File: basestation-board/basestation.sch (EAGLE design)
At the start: 68 parts, among them IC1 STM32F0, IC2 MCP1700TT, IC3 MCP73831, IC4 MCP1700TT, J2 SWD_PTH_SHROUD, Q1 BSS84, Q2 BSS84, SW1 ROTARTY_ENCODER, U1 RFM98, U2 NHD-C0216CIZ-FSW, U3 RN4020, X1 BU-SMA-V, X2 CRYSTAL-GROUNDED

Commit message: minor changes
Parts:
- added U$1: MMBZ27VCLT1, SparkFun-DiscreteSemi:MMBZ27VCLT1
- added U$2: NUP2114UCMR6T1G, Mine:NUP2114UCMR6T1G
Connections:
- new net R_INT: IC1.PB15, U1.DIO0
- net DM: now also U$2.IO1
- net DP: now also U$2.IO2
- net GND: now also U$2.VN
- net N$1: now also U$1.C
- net N$35: now also U$2.VP
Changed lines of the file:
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@@
 <part name="C17" library="resistor" deviceset="C-EU" device="C0603" value="100n"/>
 <part name="GND42" library="supply1" deviceset="GND" device=""/>
+<part name="U$1" library="SparkFun-DiscreteSemi" deviceset="MMBZ27VCLT1" device=""/>
+<part name="U$2" library="Mine" deviceset="NUP2114UCMR6T1G" device=""/>
+<part name="GND43" library="supply1" deviceset="GND" device=""/>
 </parts>
 <sheets>
@@
 <instance part="C17" gate="G$1" x="12.7" y="190.5" rot="R180"/>
 <instance part="GND42" gate="1" x="12.7" y="185.42"/>
+<instance part="U$1" gate="G$1" x="35.56" y="187.96" rot="R180"/>
+<instance part="U$2" gate="G$1" x="167.64" y="73.66"/>
+<instance part="GND43" gate="1" x="167.64" y="55.88"/>
 </instances>
 <busses>
@@
 <pinref part="U1" gate="G$1" pin="ANT"/>
 <pinref part="X1" gate="G$1" pin="1"/>
+<pinref part="U$1" gate="G$1" pin="C"/>
+<wire x1="35.56" y1="180.34" x2="35.56" y2="172.72" width="0.1524" layer="91"/>
+<junction x="35.56" y="172.72"/>
 </segment>
 </net>
@@
 <pinref part="GND42" gate="1" pin="GND"/>
 </segment>
+<segment>
+<pinref part="U$2" gate="G$1" pin="VN"/>
+<pinref part="GND43" gate="1" pin="GND"/>
+</segment>
 </net>
 <net name="VBAT_S" class="0">
@@
 <label x="119.38" y="68.58" size="1.778" layer="95"/>
 </segment>
+<segment>
+<label x="147.32" y="76.2" size="1.778" layer="95"/>
+<pinref part="U$2" gate="G$1" pin="IO1"/>
+<wire x1="157.48" y1="76.2" x2="142.24" y2="76.2" width="0.1524" layer="91"/>
+</segment>
 </net>
 <net name="DP" class="0">
@@
 <wire x1="129.54" y1="66.04" x2="116.84" y2="66.04" width="0.1524" layer="91"/>
 <label x="119.38" y="66.04" size="1.778" layer="95"/>
+</segment>
+<segment>
+<wire x1="157.48" y1="71.12" x2="142.24" y2="71.12" width="0.1524" layer="91"/>
+<label x="147.32" y="71.12" size="1.778" layer="95"/>
+<pinref part="U$2" gate="G$1" pin="IO2"/>
 </segment>
 </net>
@@
 <net name="N$35" class="0">
 <segment>
+<label x="149.86" y="88.9" size="1.778" layer="95"/>
+<pinref part="U$2" gate="G$1" pin="VP"/>
+<wire x1="129.54" y1="88.9" x2="167.64" y2="88.9" width="0.1524" layer="91"/>
 <pinref part="L1" gate="G$1" pin="2"/>
 <pinref part="JP1" gate="G$1" pin="VCC"/>
 <wire x1="121.92" y1="71.12" x2="129.54" y2="71.12" width="0.1524" layer="91"/>
+<wire x1="129.54" y1="88.9" x2="129.54" y2="71.12" width="0.1524" layer="91"/>
 </segment>
 </net>
@@
 </segment>
 </net>
+<net name="R_INT" class="0">
+<segment>
+<pinref part="U1" gate="G$1" pin="DIO0"/>
+<wire x1="35.56" y1="165.1" x2="43.18" y2="165.1" width="0.1524" layer="91"/>
+<label x="35.56" y="165.1" size="1.778" layer="95"/>
+</segment>
+<segment>
+<pinref part="IC1" gate="G$1" pin="PB15"/>
+<wire x1="43.18" y1="35.56" x2="55.88" y2="35.56" width="0.1524" layer="91"/>
+<label x="48.26" y="35.56" size="1.778" layer="95"/>
+</segment>
+</net>

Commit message: some stuff changed lol
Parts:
- removed R16: (no value), resistor:R-EU_R0603
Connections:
- net GND: no longer R16.2
- net N$28: no longer R16.1
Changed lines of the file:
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@@
 <part name="R15" library="resistor" deviceset="R-EU_" device="R0603"/>
 <part name="GND32" library="supply1" deviceset="GND" device=""/>
-<part name="R16" library="resistor" deviceset="R-EU_" device="R0603"/>
 <part name="GND33" library="supply1" deviceset="GND" device=""/>
 <part name="X2" library="SparkFun-FreqCtrl" deviceset="CRYSTAL-GROUNDED" device=""/>
@@
 <instance part="R15" gate="G$1" x="86.36" y="119.38" rot="R90"/>
 <instance part="GND32" gate="1" x="86.36" y="111.76"/>
-<instance part="R16" gate="G$1" x="121.92" y="63.5" rot="R180"/>
 <instance part="GND33" gate="1" x="114.3" y="58.42"/>
 <instance part="X2" gate="G$1" x="55.88" y="15.24" rot="R90"/>
@@
 </segment>
 <segment>
-<pinref part="R16" gate="G$1" pin="2"/>
 <wire x1="116.84" y1="63.5" x2="114.3" y2="63.5" width="0.1524" layer="91"/>
 <wire x1="114.3" y1="63.5" x2="114.3" y2="60.96" width="0.1524" layer="91"/>
@@
 <segment>
 <pinref part="JP1" gate="G$1" pin="ID"/>
-<pinref part="R16" gate="G$1" pin="1"/>
 <wire x1="129.54" y1="63.5" x2="127" y2="63.5" width="0.1524" layer="91"/>
 </segment>

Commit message: proded silk
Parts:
- removed U$1: MMBZ27VCLT1, SparkFun-DiscreteSemi:MMBZ27VCLT1
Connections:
- net N$1: no longer U$1.C
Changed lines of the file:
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@@
 <part name="C17" library="resistor" deviceset="C-EU" device="C0603" value="100n"/>
 <part name="GND42" library="supply1" deviceset="GND" device=""/>
-<part name="U$1" library="SparkFun-DiscreteSemi" deviceset="MMBZ27VCLT1" device=""/>
 <part name="U$2" library="Mine" deviceset="NUP2114UCMR6T1G" device=""/>
 <part name="GND43" library="supply1" deviceset="GND" device=""/>
@@
 <instance part="C17" gate="G$1" x="12.7" y="190.5" rot="R180"/>
 <instance part="GND42" gate="1" x="12.7" y="185.42"/>
-<instance part="U$1" gate="G$1" x="35.56" y="187.96" rot="R180"/>
 <instance part="U$2" gate="G$1" x="167.64" y="73.66"/>
 <instance part="GND43" gate="1" x="167.64" y="55.88"/>
@@
 <pinref part="U1" gate="G$1" pin="ANT"/>
 <pinref part="X1" gate="G$1" pin="1"/>
-<pinref part="U$1" gate="G$1" pin="C"/>
-<wire x1="35.56" y1="180.34" x2="35.56" y2="172.72" width="0.1524" layer="91"/>
-<junction x="35.56" y="172.72"/>
 </segment>
 </net>

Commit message: adding stuff to silk
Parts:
- C10, C13, C9: value 4u7 -> (none)
- C11: value 4u7 -> 100n
- C14, C16, C7: value (none) -> 4u7
- C17: value 100n -> 4u7
- J1: value (none) -> SWD_PTH_SHROUD; device dtb:JST_2MM_MALE -> dtb:SWD_PTH_SHROUD
- J2: value SWD_PTH_SHROUD -> (none); device dtb:SWD_PTH_SHROUD -> dtb:JST_2MM_MALE
- LED1: device led:LED5MM -> led:LEDCHIP-LED0805
- LED2: device led:LED3MM -> led:LED5MM
- LED4: device led:LEDCHIP-LED0805 -> led:LED3MM
- S1: value SWITCH-MOMENTARY-2SMD -> SWITCH-MOMENTARY-2PTH; device Mine:SWITCH-MOMENTARY-2SMD -> Mine:SWITCH-MOMENTARY-2PTH
- S3: value SWITCH-MOMENTARY-2PTH -> SWITCH-MOMENTARY-2SMD; device Mine:SWITCH-MOMENTARY-2PTH -> Mine:SWITCH-MOMENTARY-2SMD
- U1: value RFM98 -> NHD-C0216CIZ-FSW; device Mine:RFM98 -> dtb:NHD-C0216CIZ-FSW
- U2: value NHD-C0216CIZ-FSW -> RFM98; device dtb:NHD-C0216CIZ-FSW -> Mine:RFM98
- renumbered R18 to R16, U$2 to U$3, U$5 to U$1
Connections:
- removed net N$11 (its old number): LED1.C, R4.2
- new net N$10: LED4.C, R6.2
- net +3V3: now also C15.2, C17.2, C9.2, IC4.OUT, J1.VCC, R4.1, R5.1, S3.2, U1.VDD; no longer C13.2, C14.2, C6.2, IC2.OUT, J2.VCC, R6.1, R7.1, S1.2, U2.VDD
- net 3.3V: now also C11.2, C7.2, IC2.OUT, U2.3.3V; no longer C10.2, C17.2, IC4.OUT, U1.3.3V
- net AIN1: now also R11.2; no longer R15.2
- net GND: now also C14.1, J1.GND1, J1.GND2, J1.GNDD, J2.-, LED7.C, R11.1, R12.1, R6.1, S1.1, U1.K, U1.VSS, U2.GND; no longer C4.1, J1.-, J2.GND1, J2.GND2, J2.GNDD, LED4.C, R13.1, R15.1, R2.1, S3.1, U1.GND, U2.K, U2.VSS
- net LED1: now also LED3.A; no longer LED2.A
- net LED2: now also LED4.A; no longer LED3.A
- net LED3: now also LED2.A; no longer LED1.A
- net LED4: now also R2.1; no longer R4.1
- net MISO: now also U2.MISO; no longer U1.MISO
- net MOSI: now also U2.MOSI; no longer U1.MOSI
- net N$1: now also U2.ANT; no longer U1.ANT
- net N$12: now also C4.1, U1.VOUT; no longer C14.1, U2.VOUT
- net N$13: now also R8.2; no longer R11.2
- net N$15: now also LED7.A, R7.1; no longer LED5.A, R10.1
- net N$16: now also R8.1; no longer R11.1
- net N$17: now also LED5.A; no longer LED4.A
- net N$23: now also R13.1, U1.A; no longer R5.1, U2.A
- net N$27: now also R12.2, R15.1; no longer R12.1, R13.2
- net N$29: now also LED1.C; no longer LED7.C
- net N$3: now also R13.2; no longer R5.2
- net N$30: now also R10.2; no longer R17.2
- net N$31: now also C6.2; no longer C16.2
- net N$32: now also C10.2, R10.1; no longer C15.2, R17.1
- net N$33: now also C14.2, J2.+; no longer C8.2, J1.+
- net N$34: now also LED1.A, R17.2; no longer LED7.A, R8.2
- net N$4: now also S3.1; no longer S1.1
- net N$5: now also R7.2; no longer R10.2
- net N$8: now also U1.C1-; no longer U2.C1-
- net N$9: now also U1.C1+; no longer U2.C1+
- net NSS: now also U2.NSS; no longer U1.NSS
- net RST: now also J1.NRST; no longer J2.NRST
- net R_INT: now also U2.DIO0; no longer U1.DIO0
- net SCL: now also R4.2, U1.SCL; no longer R7.2, U2.SCL
- net SCLK: now also U2.SCK; no longer U1.SCK
- net SDA: now also R5.2, U1.SDA; no longer R6.2, U2.SDA
- net SW2: now also S1.2; no longer S3.2
- net SWCLK: now also J1.SWCLK; no longer J2.SWCLK
- net SWDAT: now also J1.SWDAT; no longer J2.SWDAT
- net VBAT_S: now also R15.2; no longer R12.2
- net VBUS: now also C16.2, R17.1; no longer C9.2, R8.1
- net VIN_S: now also C13.2, C8.2; no longer C11.2, C7.2
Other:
- moved on the sheet: C10, C11, C12, C13, C14, C15, C16, C17, C2, C3, C4, C5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

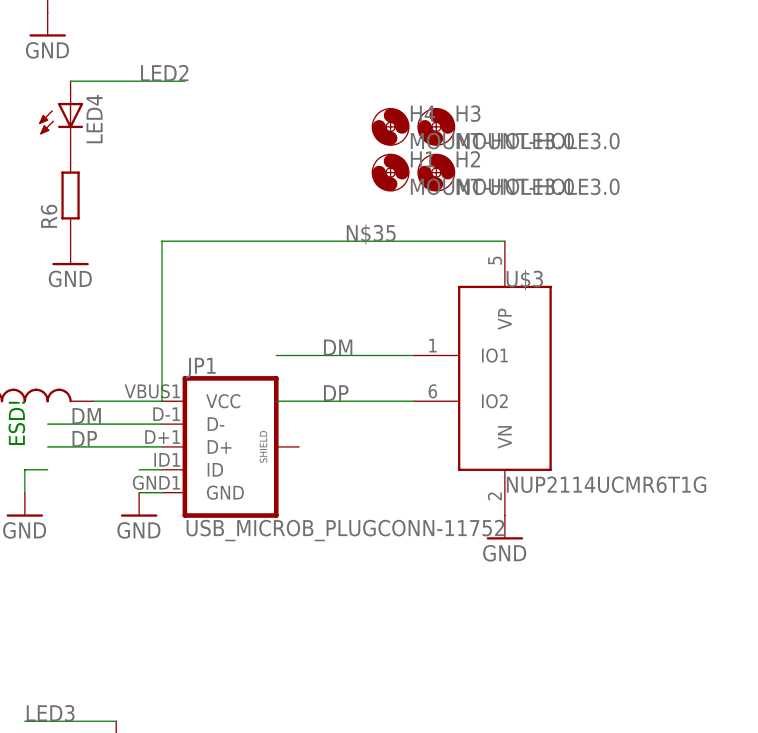
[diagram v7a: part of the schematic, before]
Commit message: added esd protection
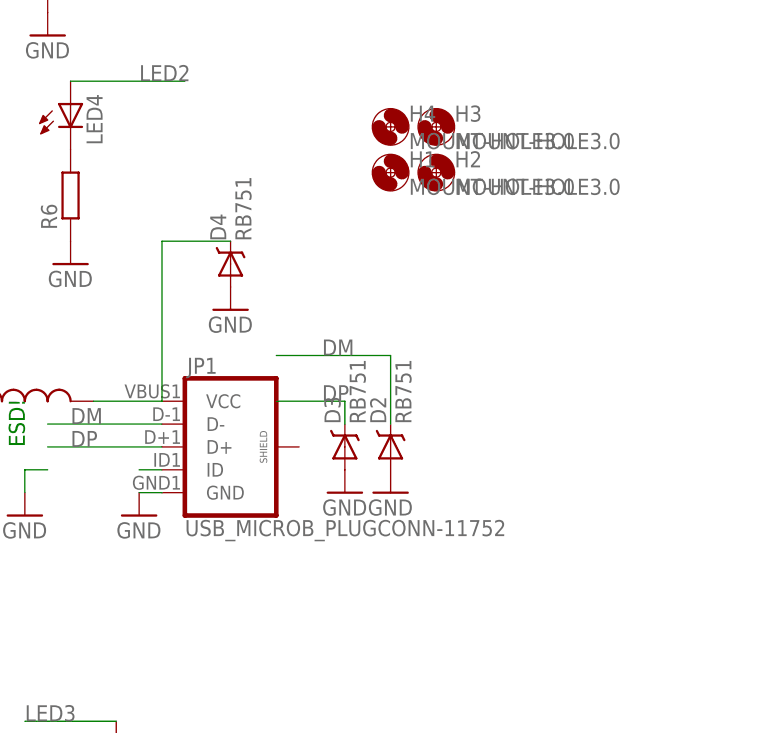
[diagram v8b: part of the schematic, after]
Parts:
- removed U$3: NUP2114UCMR6T1G, Mine:NUP2114UCMR6T1G
- added D2, D3, D4: RB751, SparkFun-DiscreteSemi:RB751
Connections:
- net DM: now also D2.C; no longer U$3.IO1
- net DP: now also D3.C; no longer U$3.IO2
- net GND: now also D2.A, D3.A, D4.A; no longer U$3.VN
- net N$35: now also D4.C; no longer U$3.VP
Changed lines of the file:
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@@
 <part name="C11" library="resistor" deviceset="C-EU" device="C0603" value="100n"/>
 <part name="GND42" library="supply1" deviceset="GND" device=""/>
-<part name="U$3" library="Mine" deviceset="NUP2114UCMR6T1G" device=""/>
-<part name="GND43" library="supply1" deviceset="GND" device=""/>
+<part name="GND44" library="supply1" deviceset="GND" device=""/>
+<part name="GND45" library="supply1" deviceset="GND" device=""/>
+<part name="D2" library="SparkFun-DiscreteSemi" deviceset="RB751" device="" value="RB751"/>
+<part name="D3" library="SparkFun-DiscreteSemi" deviceset="RB751" device="" value="RB751"/>
+<part name="D4" library="SparkFun-DiscreteSemi" deviceset="RB751" device="" value="RB751"/>
+<part name="GND46" library="supply1" deviceset="GND" device=""/>
 </parts>
 <sheets>
@@
 <instance part="C11" gate="G$1" x="12.7" y="190.5" rot="R180"/>
 <instance part="GND42" gate="1" x="12.7" y="185.42"/>
-<instance part="U$3" gate="G$1" x="167.64" y="73.66"/>
-<instance part="GND43" gate="1" x="167.64" y="55.88"/>
+<instance part="GND44" gate="1" x="137.16" y="81.28"/>
+<instance part="GND45" gate="1" x="149.86" y="60.96"/>
+<instance part="D2" gate="G$1" x="154.94" y="66.04" rot="R90"/>
+<instance part="D3" gate="G$1" x="149.86" y="66.04" rot="R90"/>
+<instance part="D4" gate="G$1" x="137.16" y="86.36" rot="R90"/>
+<instance part="GND46" gate="1" x="154.94" y="60.96"/>
 </instances>
 <busses>
@@
 </segment>
 <segment>
-<pinref part="U$3" gate="G$1" pin="VN"/>
-<pinref part="GND43" gate="1" pin="GND"/>
+<pinref part="D4" gate="G$1" pin="A"/>
+<pinref part="GND44" gate="1" pin="GND"/>
+</segment>
+<segment>
+<pinref part="D3" gate="G$1" pin="A"/>
+<pinref part="GND45" gate="1" pin="GND"/>
+</segment>
+<segment>
+<pinref part="D2" gate="G$1" pin="A"/>
+<pinref part="GND46" gate="1" pin="GND"/>
 </segment>
 </net>
@@
 <segment>
 <label x="147.32" y="76.2" size="1.778" layer="95"/>
-<pinref part="U$3" gate="G$1" pin="IO1"/>
-<wire x1="157.48" y1="76.2" x2="142.24" y2="76.2" width="0.1524" layer="91"/>
+<wire x1="154.94" y1="76.2" x2="142.24" y2="76.2" width="0.1524" layer="91"/>
+<wire x1="154.94" y1="68.58" x2="154.94" y2="76.2" width="0.1524" layer="91"/>
+<pinref part="D2" gate="G$1" pin="C"/>
 </segment>
 </net>
@@
 </segment>
 <segment>
-<wire x1="157.48" y1="71.12" x2="142.24" y2="71.12" width="0.1524" layer="91"/>
 <label x="147.32" y="71.12" size="1.778" layer="95"/>
-<pinref part="U$3" gate="G$1" pin="IO2"/>
+<wire x1="149.86" y1="71.12" x2="142.24" y2="71.12" width="0.1524" layer="91"/>
+<wire x1="149.86" y1="68.58" x2="149.86" y2="71.12" width="0.1524" layer="91"/>
+<pinref part="D3" gate="G$1" pin="C"/>
 </segment>
 </net>
@@
 <net name="N$35" class="0">
 <segment>
-<label x="149.86" y="88.9" size="1.778" layer="95"/>
-<pinref part="U$3" gate="G$1" pin="VP"/>
-<wire x1="129.54" y1="88.9" x2="167.64" y2="88.9" width="0.1524" layer="91"/>
 <pinref part="L1" gate="G$1" pin="2"/>
 <pinref part="JP1" gate="G$1" pin="VCC"/>
+<wire x1="129.54" y1="88.9" x2="137.16" y2="88.9" width="0.1524" layer="91"/>
 <wire x1="121.92" y1="71.12" x2="129.54" y2="71.12" width="0.1524" layer="91"/>
 <wire x1="129.54" y1="88.9" x2="129.54" y2="71.12" width="0.1524" layer="91"/>
-</segment>
-</net>
+<pinref part="D4" gate="G$1" pin="C"/>
+</segment>
+</net>
